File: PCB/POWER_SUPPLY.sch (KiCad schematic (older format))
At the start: 6 parts

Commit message: Updated power mixing
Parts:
- removed Q?: DMP3099L, symbol Device:Q_PMOS_DGS
- added D?: SK34BTR, symbol Device:D_Schottky
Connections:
- wire segments 22 -> 20
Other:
- moved on the sheet: BT?, D?, PS?, R?
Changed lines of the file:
@@
 L Device:Battery BT?
 U 1 1 5E90B731
-P 5350 3650
-F 0 "BT?" H 5458 3696 50  0000 L CNN
-F 1 "LEAD_ACID" H 5458 3605 50  0000 L CNN
-F 2 "" V 5350 3710 50  0001 C CNN
-F 3 "~" V 5350 3710 50  0001 C CNN
-	1    5350 3650
+P 5600 3650
+F 0 "BT?" H 5708 3696 50  0000 L CNN
+F 1 "LEAD_ACID" H 5708 3605 50  0000 L CNN
+F 2 "" V 5600 3710 50  0001 C CNN
+F 3 "~" V 5600 3710 50  0001 C CNN
+	1    5600 3650
 	1    0    0    -1
 $EndComp
 Wire Wire Line
-	4150 3200 4950 3200
-Connection ~ 5350 3200
+	4750 3200 5300 3200
+Connection ~ 5600 3200
 Wire Wire Line
-	5350 3200 5350 3450
+	5600 3200 5600 3450
 $Comp
 L power:GND #PWR?
 U 1 1 5E929E4E
-P 5350 3900
-F 0 "#PWR?" H 5350 3650 50  0001 C CNN
-F 1 "GND" H 5355 3727 50  0000 C CNN
-F 2 "" H 5350 3900 50  0001 C CNN
-F 3 "" H 5350 3900 50  0001 C CNN
-	1    5350 3900
+P 5600 3900
+F 0 "#PWR?" H 5600 3650 50  0001 C CNN
+F 1 "GND" H 5605 3727 50  0000 C CNN
+F 2 "" H 5600 3900 50  0001 C CNN
+F 3 "" H 5600 3900 50  0001 C CNN
+	1    5600 3900
 	1    0    0    -1
 $EndComp
 Wire Wire Line
-	5350 3900 5350 3850
+	5600 3900 5600 3850
 Wire Wire Line
-	3200 2650 3400 2650
+	3750 2850 3950 2850
 Wire Wire Line
-	3500 3200 3400 3200
+	4100 3200 3950 3200
 Wire Wire Line
-	3400 3200 3400 2650
-Connection ~ 3400 2650
+	3950 3200 3950 2850
+Connection ~ 3950 2850
 $Comp
 L power:GND #PWR?
 U 1 1 5E92F162
-P 3250 2900
-F 0 "#PWR?" H 3250 2650 50  0001 C CNN
-F 1 "GND" H 3255 2727 50  0000 C CNN
-F 2 "" H 3250 2900 50  0001 C CNN
-F 3 "" H 3250 2900 50  0001 C CNN
-	1    3250 2900
+P 3800 3100
+F 0 "#PWR?" H 3800 2850 50  0001 C CNN
+F 1 "GND" H 3805 2927 50  0000 C CNN
+F 2 "" H 3800 3100 50  0001 C CNN
+F 3 "" H 3800 3100 50  0001 C CNN
+	1    3800 3100
 	1    0    0    -1
 $EndComp
 Wire Wire Line
-	3200 2850 3250 2850
+	3750 3050 3800 3050
 Wire Wire Line
-	3250 2850 3250 2900
+	3800 3050 3800 3100
 Wire Wire Line
-	6100 2650 6100 3200
+	6100 2850 6100 3200
 Connection ~ 6100 3200
 Wire Wire Line
@@
 L Converter_ACDC:IRM-20-15 PS?
 U 1 1 5E92C858
-P 2800 2750
-F 0 "PS?" H 2800 3075 50  0000 C CNN
-F 1 "IRM-30-15" H 2800 2984 50  0000 C CNN
-F 2 "" H 2800 2450 50  0001 C CNN
-F 3 "https://www.meanwell.com/Upload/PDF/IRM-30/IRM-30-SPEC.PDF" H 3200 2400 50  0001 C CNN
-	1    2800 2750
+P 3350 2950
+F 0 "PS?" H 3350 3275 50  0000 C CNN
+F 1 "IRM-30-15" H 3350 3184 50  0000 C CNN
+F 2 "" H 3350 2650 50  0001 C CNN
+F 3 "https://www.meanwell.com/Upload/PDF/IRM-30/IRM-30-SPEC.PDF" H 3750 2600 50  0001 C CNN
+	1    3350 2950
 	1    0    0    -1
 $EndComp
 Wire Wire Line
-	5900 3200 6100 3200
-Wire Wire Line
-	5350 3200 5500 3200
-Wire Wire Line
-	5750 2650 5700 2650
-Wire Wire Line
-	3400 2650 5700 2650
-Connection ~ 5700 2650
-Wire Wire Line
-	5700 2650 5700 2900
-$Comp
-L Device:Q_PMOS_DGS Q?
-U 1 1 5E90FAA8
-P 5700 3100
-F 0 "Q?" V 5949 3100 50  0000 C CNN
-F 1 "DMP3099L" V 6040 3100 50  0000 C CNN
-F 2 "" H 5900 3200 50  0001 C CNN
-F 3 "https://www.diodes.com/assets/Datasheets/DMP3099L.pdf" H 5700 3100 50  0001 C CNN
-	1    5700 3100
-	0    1    1    0
-$EndComp
+	6000 3200 6100 3200
 $Comp
 L Device:D_Schottky D?
 U 1 1 5E96E6B3
-P 5900 2650
-F 0 "D?" H 5900 2434 50  0000 C CNN
-F 1 "SK34BTR" H 5900 2525 50  0000 C CNN
-F 2 "" H 5900 2650 50  0001 C CNN
-F 3 "http://www.smc-diodes.com/propdf/SK34B%20N0935%20REV.C.pdf" H 5900 2650 50  0001 C CNN
-	1    5900 2650
+P 5850 2850
+F 0 "D?" H 5850 2634 50  0000 C CNN
+F 1 "SK34BTR" H 5850 2725 50  0000 C CNN
+F 2 "" H 5850 2850 50  0001 C CNN
+F 3 "http://www.smc-diodes.com/propdf/SK34B%20N0935%20REV.C.pdf" H 5850 2850 50  0001 C CNN
+	1    5850 2850
 	-1   0    0    1
 $EndComp
 Wire Wire Line
-	6050 2650 6100 2650
-Text HLabel 2400 2650 0    50   Input ~ 0
+	6000 2850 6100 2850
+Text HLabel 2950 2850 0    50   Input ~ 0
 AC_LIVE
-Text HLabel 2400 2850 0    50   Input ~ 0
+Text HLabel 2950 3050 0    50   Input ~ 0
 AC_NEUTRAL
 Text HLabel 7050 3200 2    50   Output ~ 0
 12V
-Text HLabel 4900 3600 0    50   Output ~ 0
+Text HLabel 5250 3600 0    50   Output ~ 0
 VBATT_SENSE
 $Comp
 L Device:R_Small R?
 U 1 1 5E987A48
-P 4950 3750
-F 0 "R?" H 5009 3796 50  0000 L CNN
-F 1 "10k" H 5009 3705 50  0000 L CNN
-F 2 "" H 4950 3750 50  0001 C CNN
-F 3 "~" H 4950 3750 50  0001 C CNN
-	1    4950 3750
+P 5300 3750
+F 0 "R?" H 5359 3796 50  0000 L CNN
+F 1 "10k" H 5359 3705 50  0000 L CNN
+F 2 "" H 5300 3750 50  0001 C CNN
+F 3 "~" H 5300 3750 50  0001 C CNN
+	1    5300 3750
 	1    0    0    -1
 $EndComp
 Wire Wire Line
-	4900 3600 4950 3600
+	5250 3600 5300 3600
 Wire Wire Line
-	4950 3600 4950 3550
+	5300 3600 5300 3550
 Wire Wire Line
-	4950 3650 4950 3600
-Connection ~ 4950 3600
+	5300 3650 5300 3600
+Connection ~ 5300 3600
 $Comp
 L power:GND #PWR?
 U 1 1 5E989430
-P 4950 3900
-F 0 "#PWR?" H 4950 3650 50  0001 C CNN
-F 1 "GND" H 4955 3727 50  0000 C CNN
-F 2 "" H 4950 3900 50  0001 C CNN
-F 3 "" H 4950 3900 50  0001 C CNN
-	1    4950 3900
+P 5300 3900
+F 0 "#PWR?" H 5300 3650 50  0001 C CNN
+F 1 "GND" H 5305 3727 50  0000 C CNN
+F 2 "" H 5300 3900 50  0001 C CNN
+F 3 "" H 5300 3900 50  0001 C CNN
+	1    5300 3900
 	1    0    0    -1
 $EndComp
 Wire Wire Line
-	4950 3850 4950 3900
+	5300 3850 5300 3900
 $Comp
 L Device:R_Small R?
 U 1 1 5E98794C
-P 4950 3450
-F 0 "R?" H 5009 3496 50  0000 L CNN
-F 1 "56k" H 5009 3405 50  0000 L CNN
-F 2 "" H 4950 3450 50  0001 C CNN
-F 3 "~" H 4950 3450 50  0001 C CNN
-	1    4950 3450
+P 5300 3450
+F 0 "R?" H 5359 3496 50  0000 L CNN
+F 1 "56k" H 5359 3405 50  0000 L CNN
+F 2 "" H 5300 3450 50  0001 C CNN
+F 3 "~" H 5300 3450 50  0001 C CNN
+	1    5300 3450
 	1    0    0    -1
 $EndComp
 Wire Wire Line
-	4950 3200 4950 3350
-Connection ~ 4950 3200
+	5300 3200 5300 3350
+Connection ~ 5300 3200
 Wire Wire Line
-	4950 3200 5350 3200
+	5300 3200 5600 3200
 $Sheet
-S 3500 3100 650  200
+S 4100 3100 650  200
 U 5E99291C
 F0 "SLA Charger" 50
 F1 "LM317_SLA_CHARGER.sch" 50
-F2 "VIN" I L 3500 3200 50
-F3 "VBATT" O R 4150 3200 50
+F2 "VIN" I L 4100 3200 50
+F3 "VBATT" O R 4750 3200 50
 $EndSheet
+Wire Wire Line
+	3950 2850 5700 2850
+$Comp
+L Device:D_Schottky D?
+U 1 1 5E99D1CB
+P 5850 3200
+F 0 "D?" H 5850 2984 50  0000 C CNN
+F 1 "SK34BTR" H 5850 3075 50  0000 C CNN
+F 2 "" H 5850 3200 50  0001 C CNN
+F 3 "http://www.smc-diodes.com/propdf/SK34B%20N0935%20REV.C.pdf" H 5850 3200 50  0001 C CNN
+	1    5850 3200
+	-1   0    0    1
+$EndComp
+Wire Wire Line
+	5600 3200 5700 3200
 $EndSCHEMATC

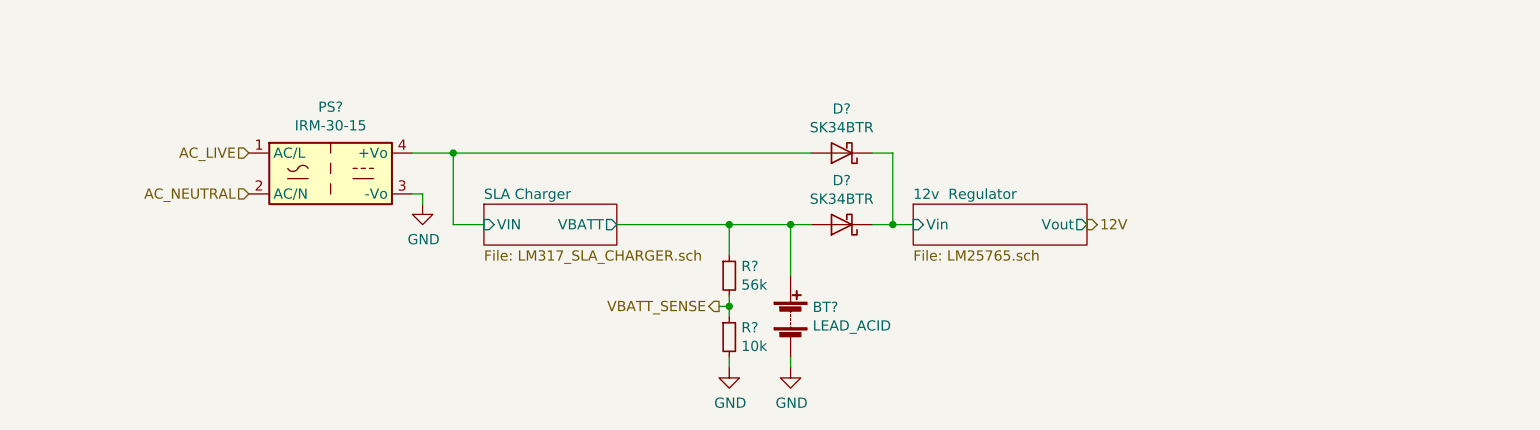
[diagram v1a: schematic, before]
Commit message: Added 3V3 regulator
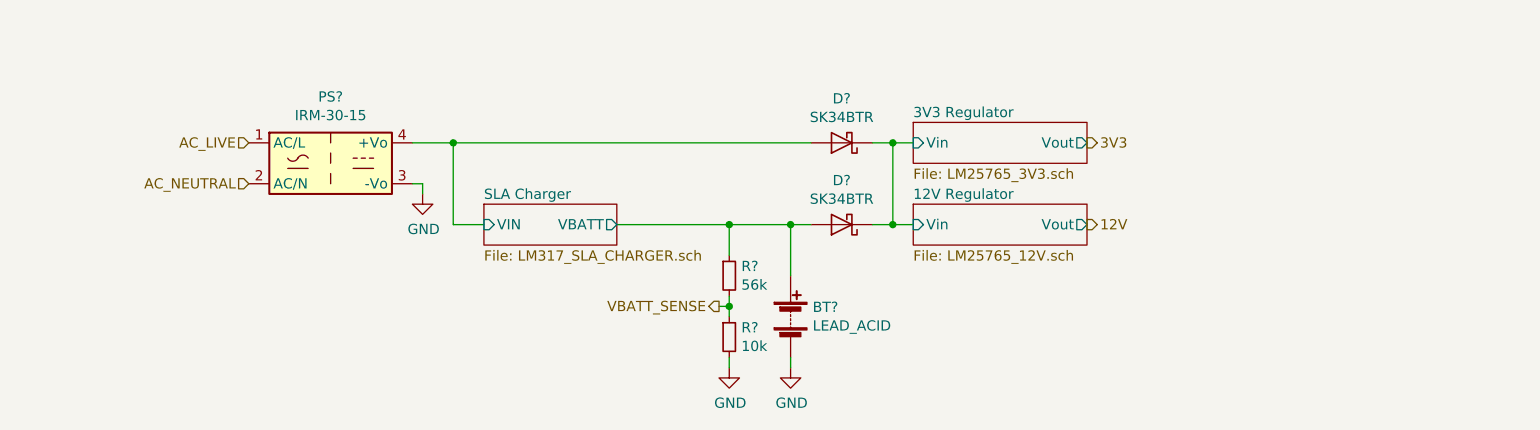
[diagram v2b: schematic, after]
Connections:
- net 12v  Regulator/Vin renamed 12V Regulator/Vin
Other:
- moved on the sheet: D?, PS?
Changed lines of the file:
@@
 $Descr A4 11693 8268
 encoding utf-8
-Sheet 9 20
+Sheet 9 21
 Title ""
 Date ""
@@
 Comment4 ""
 $EndDescr
-$Sheet
-S 6200 3100 850  200
-U 5E904307
-F0 "12v  Regulator" 50
-F1 "LM25765.sch" 50
-F2 "Vin" I L 6200 3200 50
-F3 "Vout" O R 7050 3200 50
-$EndSheet
 $Comp
 L Device:Battery BT?
@@
 	5600 3900 5600 3850
 Wire Wire Line
-	3750 2850 3950 2850
+	3750 2800 3950 2800
 Wire Wire Line
 	4100 3200 3950 3200
 Wire Wire Line
-	3950 3200 3950 2850
-Connection ~ 3950 2850
+	3950 3200 3950 2800
+Connection ~ 3950 2800
 $Comp
 L power:GND #PWR?
 U 1 1 5E92F162
-P 3800 3100
-F 0 "#PWR?" H 3800 2850 50  0001 C CNN
-F 1 "GND" H 3805 2927 50  0000 C CNN
-F 2 "" H 3800 3100 50  0001 C CNN
-F 3 "" H 3800 3100 50  0001 C CNN
-	1    3800 3100
+P 3800 3050
+F 0 "#PWR?" H 3800 2800 50  0001 C CNN
+F 1 "GND" H 3805 2877 50  0000 C CNN
+F 2 "" H 3800 3050 50  0001 C CNN
+F 3 "" H 3800 3050 50  0001 C CNN
+	1    3800 3050
 	1    0    0    -1
 $EndComp
 Wire Wire Line
-	3750 3050 3800 3050
+	3750 3000 3800 3000
 Wire Wire Line
-	3800 3050 3800 3100
+	3800 3000 3800 3050
 Wire Wire Line
-	6100 2850 6100 3200
+	6100 2800 6100 3200
 Connection ~ 6100 3200
 Wire Wire Line
@@
 L Converter_ACDC:IRM-20-15 PS?
 U 1 1 5E92C858
-P 3350 2950
-F 0 "PS?" H 3350 3275 50  0000 C CNN
-F 1 "IRM-30-15" H 3350 3184 50  0000 C CNN
-F 2 "" H 3350 2650 50  0001 C CNN
-F 3 "https://www.meanwell.com/Upload/PDF/IRM-30/IRM-30-SPEC.PDF" H 3750 2600 50  0001 C CNN
-	1    3350 2950
+P 3350 2900
+F 0 "PS?" H 3350 3225 50  0000 C CNN
+F 1 "IRM-30-15" H 3350 3134 50  0000 C CNN
+F 2 "" H 3350 2600 50  0001 C CNN
+F 3 "https://www.meanwell.com/Upload/PDF/IRM-30/IRM-30-SPEC.PDF" H 3750 2550 50  0001 C CNN
+	1    3350 2900
 	1    0    0    -1
 $EndComp
@@
 L Device:D_Schottky D?
 U 1 1 5E96E6B3
-P 5850 2850
-F 0 "D?" H 5850 2634 50  0000 C CNN
-F 1 "SK34BTR" H 5850 2725 50  0000 C CNN
-F 2 "" H 5850 2850 50  0001 C CNN
-F 3 "http://www.smc-diodes.com/propdf/SK34B%20N0935%20REV.C.pdf" H 5850 2850 50  0001 C CNN
-	1    5850 2850
+P 5850 2800
+F 0 "D?" H 5850 2584 50  0000 C CNN
+F 1 "SK34BTR" H 5850 2675 50  0000 C CNN
+F 2 "" H 5850 2800 50  0001 C CNN
+F 3 "http://www.smc-diodes.com/propdf/SK34B%20N0935%20REV.C.pdf" H 5850 2800 50  0001 C CNN
+	1    5850 2800
 	-1   0    0    1
 $EndComp
 Wire Wire Line
-	6000 2850 6100 2850
-Text HLabel 2950 2850 0    50   Input ~ 0
+	6000 2800 6100 2800
+Text HLabel 2950 2800 0    50   Input ~ 0
 AC_LIVE
-Text HLabel 2950 3050 0    50   Input ~ 0
+Text HLabel 2950 3000 0    50   Input ~ 0
 AC_NEUTRAL
 Text HLabel 7050 3200 2    50   Output ~ 0
@@
 $EndSheet
 Wire Wire Line
-	3950 2850 5700 2850
+	3950 2800 5700 2800
 $Comp
 L Device:D_Schottky D?
@@
 Wire Wire Line
 	5600 3200 5700 3200
+Text HLabel 7050 2800 2    50   Output ~ 0
+3V3
+$Sheet
+S 6200 2700 850  200
+U 5E9C913B
+F0 "3V3 Regulator" 50
+F1 "LM25765_3V3.sch" 50
+F2 "Vout" O R 7050 2800 50
+F3 "Vin" I L 6200 2800 50
+$EndSheet
+$Sheet
+S 6200 3100 850  200
+U 5E9C98F5
+F0 "12V Regulator" 50
+F1 "LM25765_12V.sch" 50
+F2 "Vout" O R 7050 3200 50
+F3 "Vin" I L 6200 3200 50
+$EndSheet
+Wire Wire Line
+	6200 2800 6100 2800
+Connection ~ 6100 2800
 $EndSCHEMATC

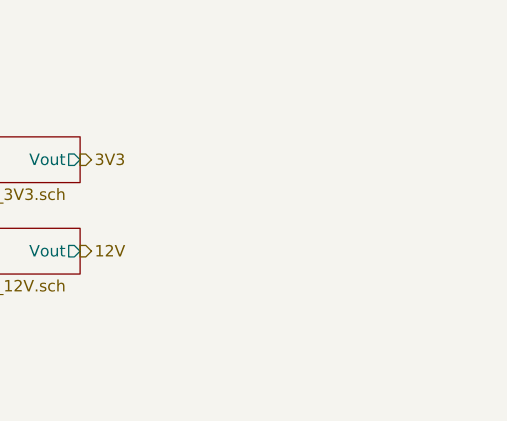
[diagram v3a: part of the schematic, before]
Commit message: Added Power LEDs
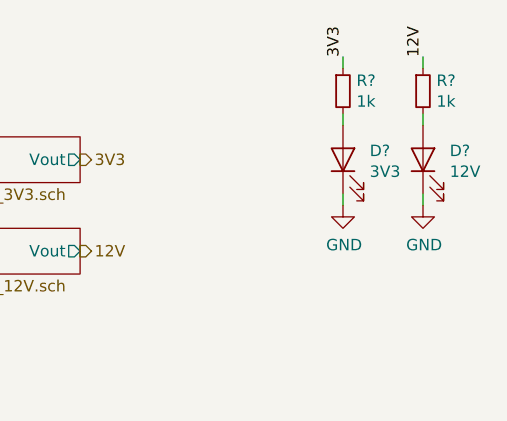
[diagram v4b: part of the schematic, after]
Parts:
- added D?: 3V3, symbol Device:LED
- added D?: 12V, symbol Device:LED
- added R? (x2): 1k, symbol Device:R_Small
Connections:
- net 12V: now also R?.1
- net 3V3: now also R?.1
- net GND: now also D?.1 (K), D?.1 (K)
- new net: D?.2 (A), R?.2 (x2)
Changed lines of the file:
@@
 Wire Wire Line
 	6100 2800 6100 3200
-Connection ~ 6100 3200
-Wire Wire Line
-	6100 3200 6200 3200
 $Comp
 L Converter_ACDC:IRM-20-15 PS?
@@
 	6200 2800 6100 2800
 Connection ~ 6100 2800
+$Comp
+L Device:LED D?
+U 1 1 5E8B2580
+P 8200 2800
+F 0 "D?" V 8239 2683 50  0000 R CNN
+F 1 "3V3" V 8148 2683 50  0000 R CNN
+F 2 "" H 8200 2800 50  0001 C CNN
+F 3 "~" H 8200 2800 50  0001 C CNN
+	1    8200 2800
+	0    -1   -1   0
+$EndComp
+$Comp
+L Device:R_Small R?
+U 1 1 5E8B32F4
+P 8200 2500
+F 0 "R?" H 8259 2546 50  0000 L CNN
+F 1 "1k" H 8259 2455 50  0000 L CNN
+F 2 "" H 8200 2500 50  0001 C CNN
+F 3 "~" H 8200 2500 50  0001 C CNN
+	1    8200 2500
+	1    0    0    -1
+$EndComp
+Wire Wire Line
+	8200 2600 8200 2650
+$Comp
+L power:GND #PWR?
+U 1 1 5E8B38F1
+P 8200 3000
+F 0 "#PWR?" H 8200 2750 50  0001 C CNN
+F 1 "GND" H 8205 2827 50  0000 C CNN
+F 2 "" H 8200 3000 50  0001 C CNN
+F 3 "" H 8200 3000 50  0001 C CNN
+	1    8200 3000
+	1    0    0    -1
+$EndComp
+Wire Wire Line
+	8200 2950 8200 3000
+$Comp
+L Device:LED D?
+U 1 1 5E8B5AE6
+P 8550 2800
+F 0 "D?" V 8589 2683 50  0000 R CNN
+F 1 "12V" V 8498 2683 50  0000 R CNN
+F 2 "" H 8550 2800 50  0001 C CNN
+F 3 "~" H 8550 2800 50  0001 C CNN
+	1    8550 2800
+	0    -1   -1   0
+$EndComp
+$Comp
+L Device:R_Small R?
+U 1 1 5E8B5AEC
+P 8550 2500
+F 0 "R?" H 8609 2546 50  0000 L CNN
+F 1 "1k" H 8609 2455 50  0000 L CNN
+F 2 "" H 8550 2500 50  0001 C CNN
+F 3 "~" H 8550 2500 50  0001 C CNN
+	1    8550 2500
+	1    0    0    -1
+$EndComp
+Wire Wire Line
+	8550 2600 8550 2650
+$Comp
+L power:GND #PWR?
+U 1 1 5E8B5AF3
+P 8550 3000
+F 0 "#PWR?" H 8550 2750 50  0001 C CNN
+F 1 "GND" H 8555 2827 50  0000 C CNN
+F 2 "" H 8550 3000 50  0001 C CNN
+F 3 "" H 8550 3000 50  0001 C CNN
+	1    8550 3000
+	1    0    0    -1
+$EndComp
+Wire Wire Line
+	8550 2950 8550 3000
+Text Label 8200 2350 1    50   ~ 0
+3V3
+Wire Wire Line
+	8200 2350 8200 2400
+Text Label 8550 2350 1    50   ~ 0
+12V
+Wire Wire Line
+	8550 2350 8550 2400
+Connection ~ 6100 3200
+Wire Wire Line
+	6100 3200 6200 3200
 $EndSCHEMATC

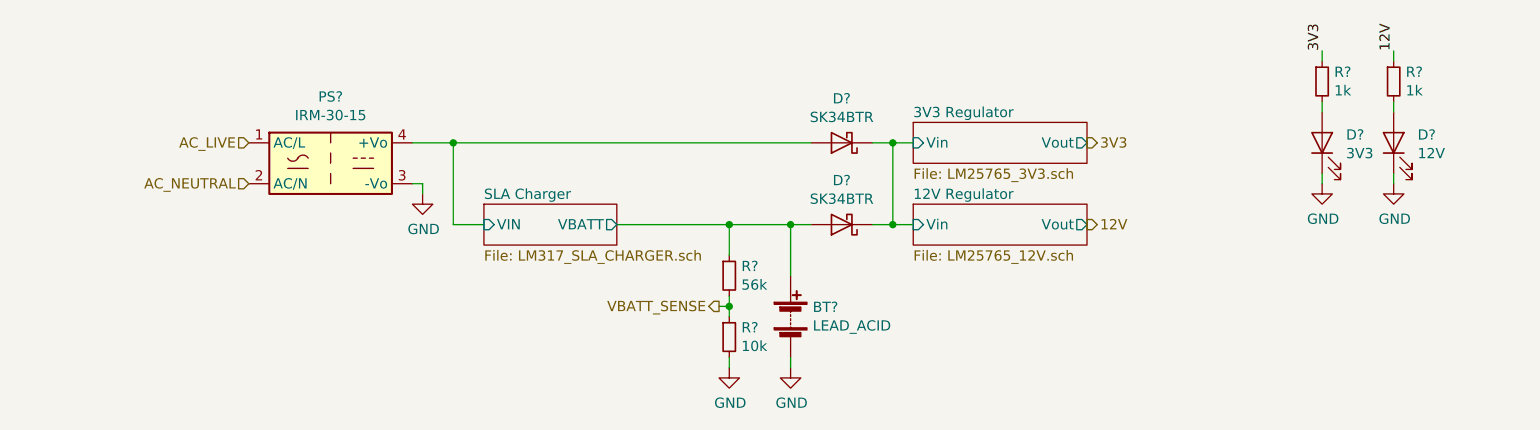
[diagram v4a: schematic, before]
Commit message: Added additional power LED
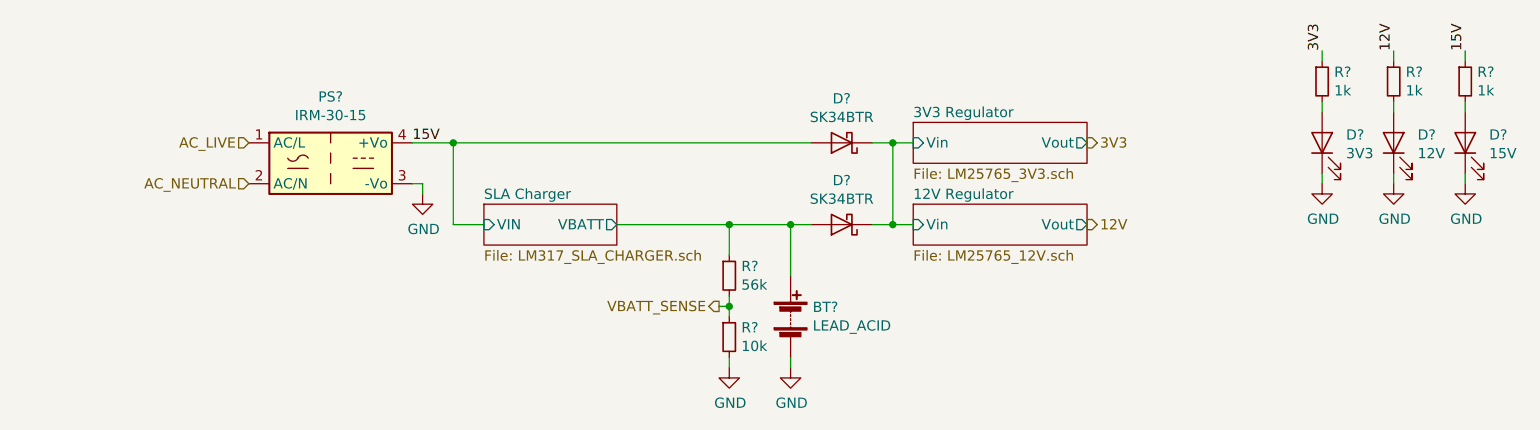
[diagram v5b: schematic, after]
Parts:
- added D?: 15V, symbol Device:LED
- added R?: 1k, symbol Device:R_Small
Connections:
- net GND: now also D?.1 (K)
- net SLA Charger/VIN renamed 15V
- net 15V: now also R?.1
- new net: D?.2 (A), R?.2
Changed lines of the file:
@@
 Wire Wire Line
 	6100 3200 6200 3200
+$Comp
+L Device:LED D?
+U 1 1 5E8B6ACE
+P 8900 2800
+F 0 "D?" V 8939 2683 50  0000 R CNN
+F 1 "15V" V 8848 2683 50  0000 R CNN
+F 2 "" H 8900 2800 50  0001 C CNN
+F 3 "~" H 8900 2800 50  0001 C CNN
+	1    8900 2800
+	0    -1   -1   0
+$EndComp
+$Comp
+L Device:R_Small R?
+U 1 1 5E8B6AD4
+P 8900 2500
+F 0 "R?" H 8959 2546 50  0000 L CNN
+F 1 "1k" H 8959 2455 50  0000 L CNN
+F 2 "" H 8900 2500 50  0001 C CNN
+F 3 "~" H 8900 2500 50  0001 C CNN
+	1    8900 2500
+	1    0    0    -1
+$EndComp
+Wire Wire Line
+	8900 2600 8900 2650
+$Comp
+L power:GND #PWR?
+U 1 1 5E8B6ADB
+P 8900 3000
+F 0 "#PWR?" H 8900 2750 50  0001 C CNN
+F 1 "GND" H 8905 2827 50  0000 C CNN
+F 2 "" H 8900 3000 50  0001 C CNN
+F 3 "" H 8900 3000 50  0001 C CNN
+	1    8900 3000
+	1    0    0    -1
+$EndComp
+Wire Wire Line
+	8900 2950 8900 3000
+Text Label 8900 2350 1    50   ~ 0
+15V
+Wire Wire Line
+	8900 2350 8900 2400
+Text Label 3750 2800 0    50   ~ 0
+15V
 $EndSCHEMATC
